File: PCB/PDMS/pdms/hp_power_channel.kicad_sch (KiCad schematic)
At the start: 0 parts

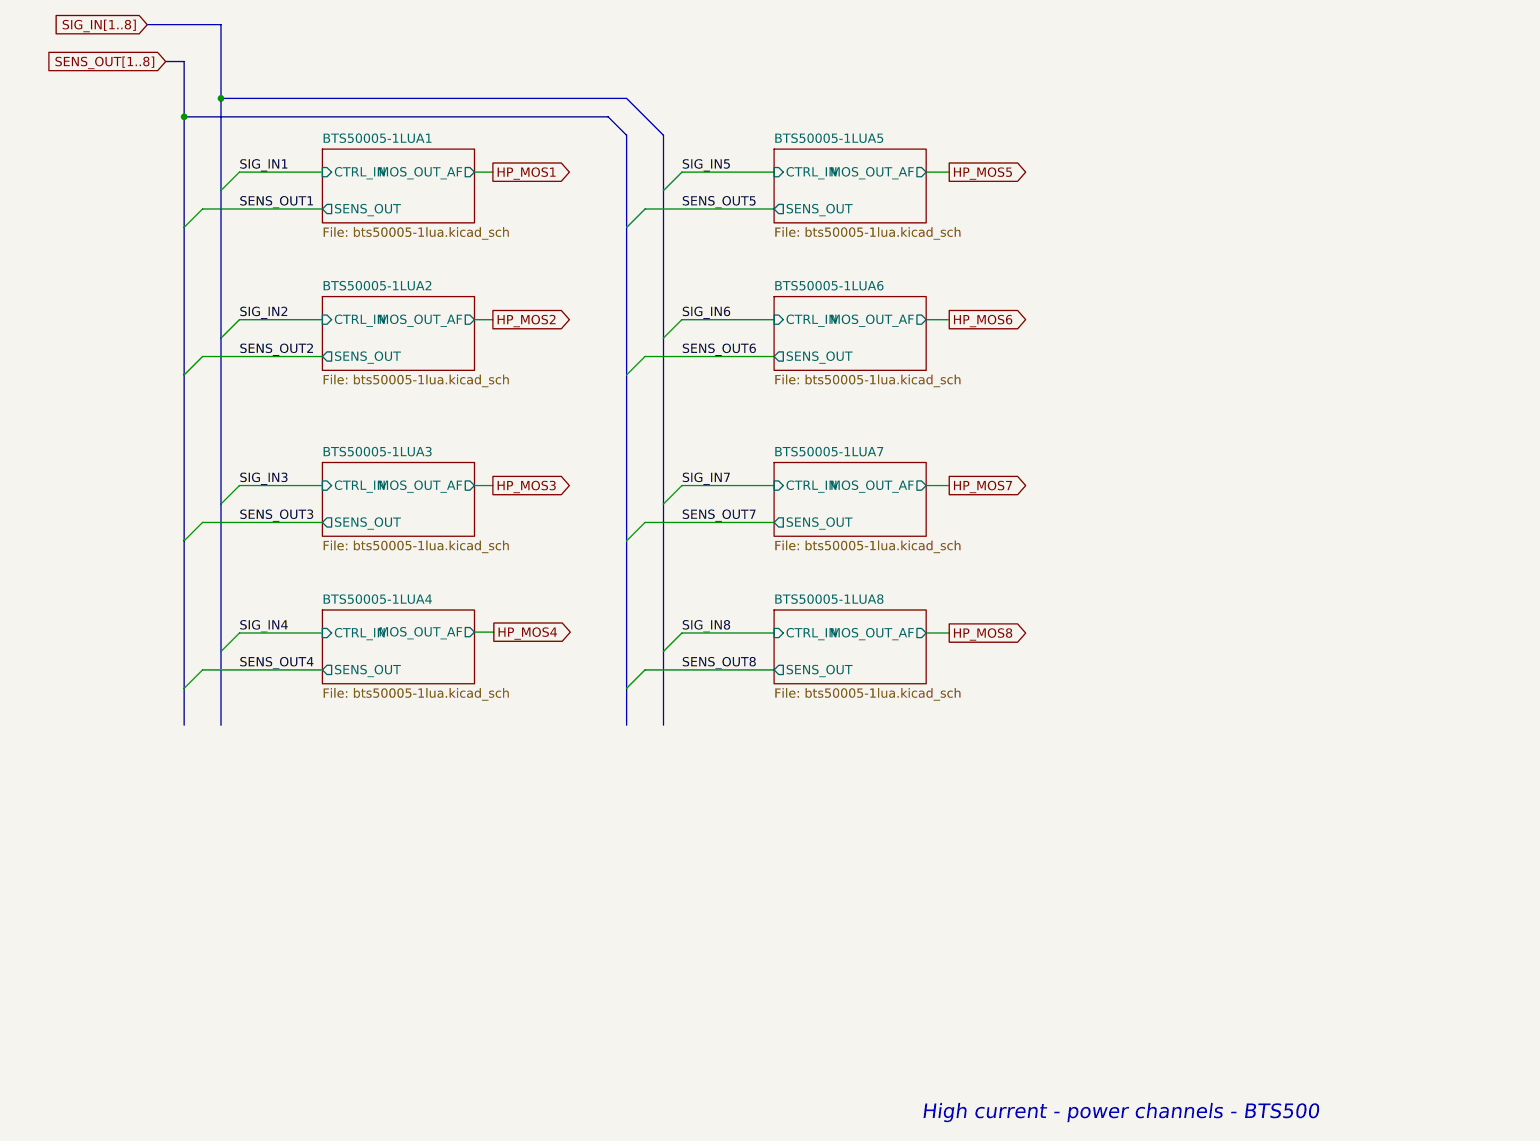
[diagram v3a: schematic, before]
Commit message: WIP PCB folder structure and schematic clean-up
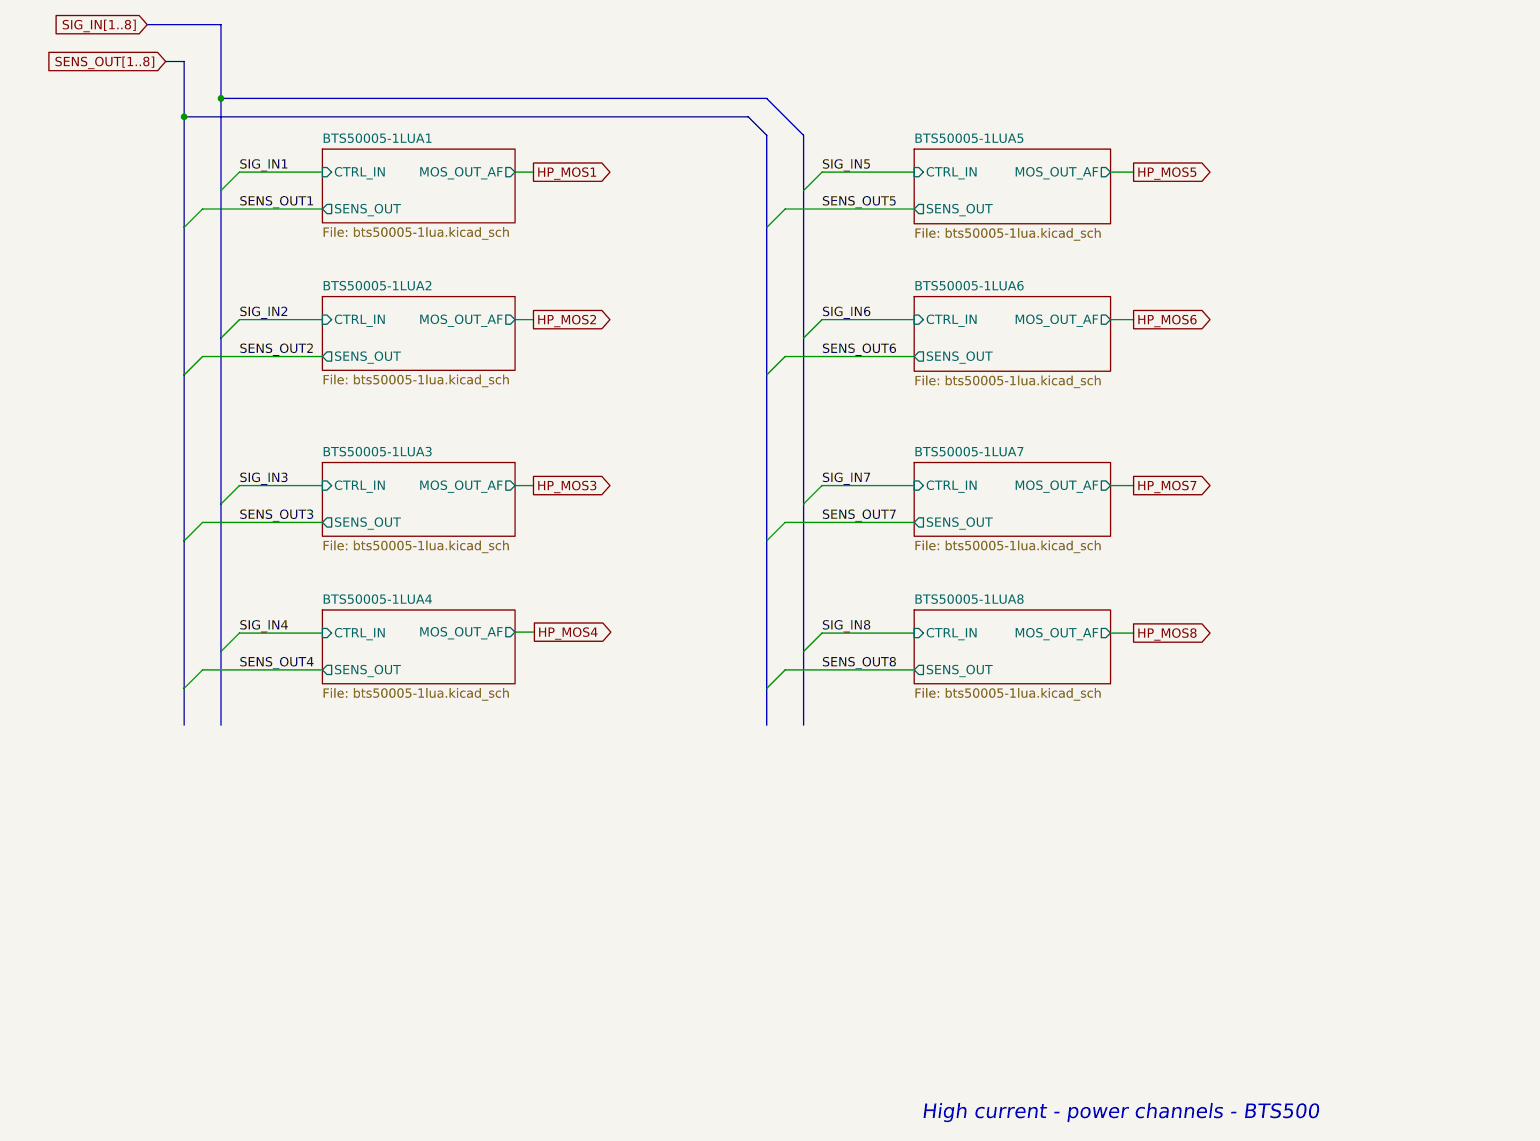
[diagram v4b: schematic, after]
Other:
- company: (none) -> PGRacing Team
